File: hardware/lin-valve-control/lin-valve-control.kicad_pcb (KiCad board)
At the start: 4 copper layers, 55.6 x 43.2 mm, 65 parts, among them J1 UPDI, J2 I2C LCD, J3 Screw_Terminal_01x03, J4 Screw_Terminal_01x05, Q1 2N7002, Q2 2N7002, U1 TJA1021T, U2 ATtiny824-X, U3 PCA9536DP, U4 LTC3203BEDD-PBF, U5 BD9G341EFJ, U6 TCA9534, U7 DRV8801PWP

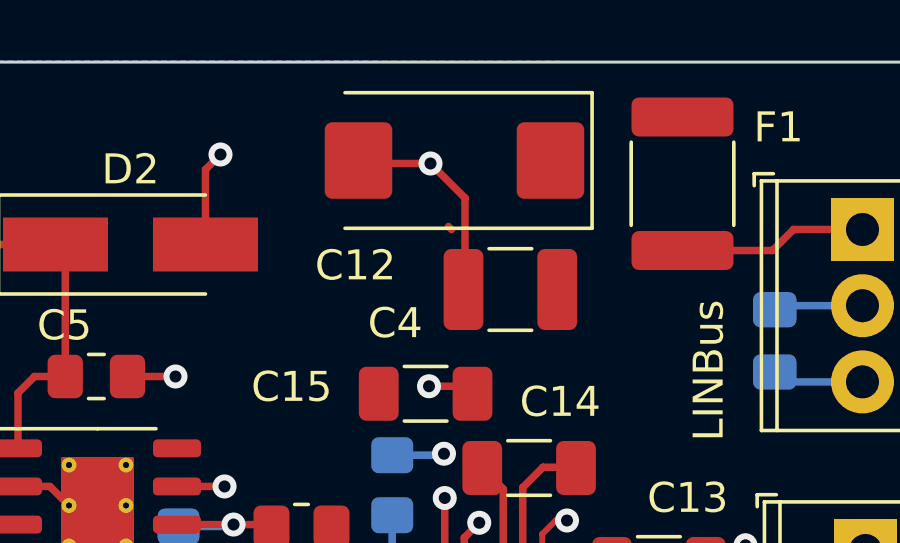
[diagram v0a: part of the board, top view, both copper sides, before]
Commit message: Add firmware for lin-coolant-temperature, cleanup layout
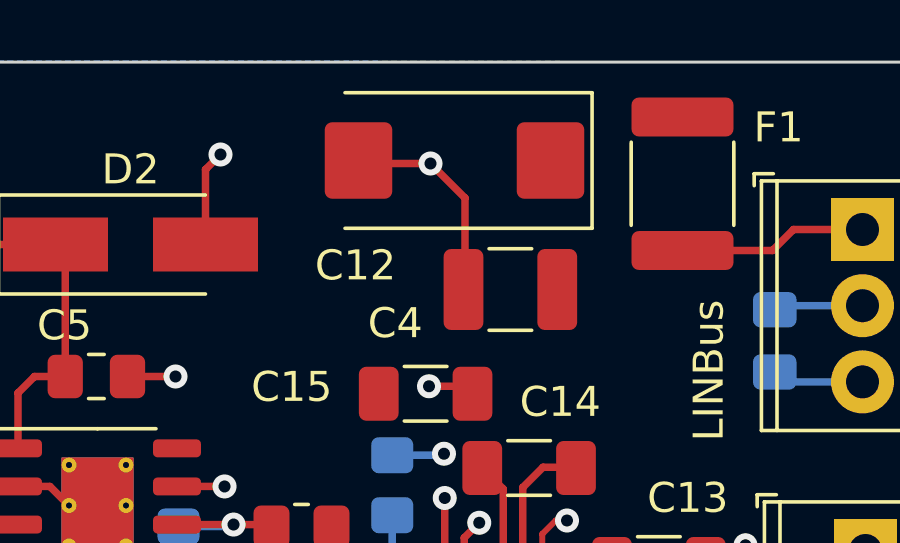
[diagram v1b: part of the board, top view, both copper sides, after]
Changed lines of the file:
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@@
   (segment (start 218.925 97.85) (end 218.9 97.875) (width 0.25) (layer "F.Cu") (net 20))
   (segment (start 218.9 97.875) (end 216.4 97.875) (width 0.25) (layer "F.Cu") (net 20))
-  (segment (start 211 64) (end 210.9 63.9) (width 0.25) (layer "F.Cu") (net 21))
   (segment (start 216.4 91.84) (end 216.36 91.8) (width 0.25) (layer "F.Cu") (net 22))
   (segment (start 216.4 94.575) (end 216.4 91.84) (width 0.25) (layer "F.Cu") (net 22))

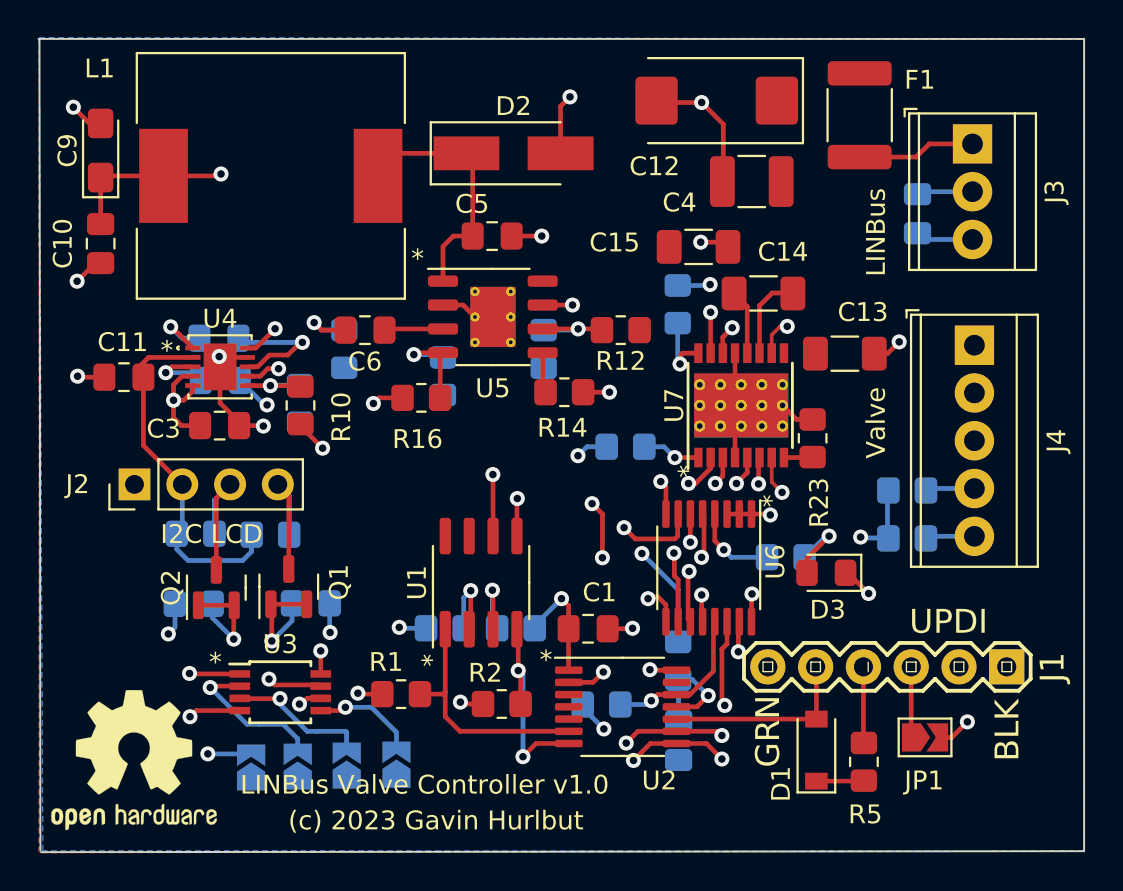
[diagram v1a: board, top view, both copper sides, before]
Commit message: Rework valve-controller board, simplify firmware
- linbus_interface and linbus_registers moved to the common lib.
- reworked them all to compile again
- removing PCA9536 from all boards, adding the voltage reg. module
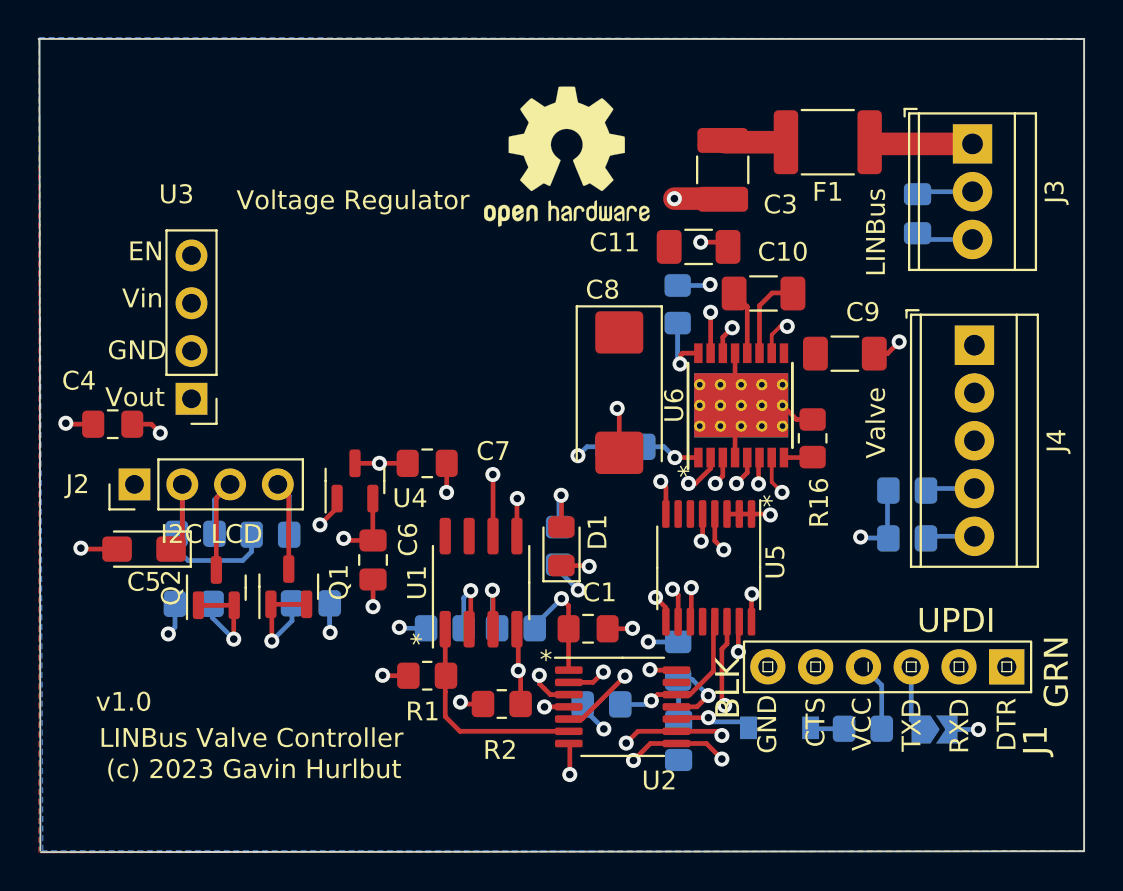
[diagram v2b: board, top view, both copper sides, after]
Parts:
- removed the C10 at (178.3, 69.3)
- removed the C11 at (179.6, 76.4)
- removed the C8 at (184.6, 74.3)
- removed the C9 at (178.3, 64.3)
- removed the D2 at (200.3, 64.5)
- removed D3: LED, LED_SMD:LED_0805_2012Metric_Pad1.15x1.40mm_HandSolder
- removed JP2: A3, Jumper:SolderJumper-2_P1.3mm_Open_TrianglePad1.0x1.5mm
- removed JP3: A2, Jumper:SolderJumper-2_P1.3mm_Open_TrianglePad1.0x1.5mm
- removed JP4: A1, Jumper:SolderJumper-2_P1.3mm_Open_TrianglePad1.0x1.5mm
- removed JP5: A0, Jumper:SolderJumper-2_P1.3mm_Open_TrianglePad1.0x1.5mm
- removed L1: 33uH 5A 88mOhm, Beirdo:PM4346.333NLT
- removed the R10 at (189.0, 77.9)
- removed the R11 at (188.9, 77.8)
- removed the R12 at (206.0, 73.9)
- removed the R13 at (201.9, 74.9)
- removed the R14 at (203.0, 77.2)
- removed the R15 at (191.3, 74.9)
- removed the R16 at (195.4, 77.5)
- removed the R17 at (196.6, 76.3)
- removed R25: 330, Resistor_SMD:R_0805_2012Metric_Pad1.20x1.40mm_HandSolder
- removed the U5 at (199.2, 73.2)
- added D1: LED, LED_SMD:LED_0805_2012Metric_Pad1.15x1.40mm_HandSolder, F.Cu at (202.8, 85.4)
- added R5: 330, Resistor_SMD:R_0805_2012Metric_Pad1.20x1.40mm_HandSolder, B.Cu at (202.7, 85.4)
- C3: value 2.2uF -> 10uF 100V; footprint Capacitor_SMD:C_0805_2012Metric_Pad1.18x1.45mm_HandSolder -> Capacitor_SMD:C_1210_3225Metric_Pad1.33x2.70mm_HandSolder
- C4: value 10uF 100V -> 1uF; footprint Capacitor_SMD:C_1210_3225Metric_Pad1.33x2.70mm_HandSolder -> Capacitor_SMD:C_0805_2012Metric_Pad1.18x1.45mm_HandSolder
- C5: value 100nF -> 100uF Ta 6V; footprint Capacitor_SMD:C_0805_2012Metric_Pad1.18x1.45mm_HandSolder -> Capacitor_Tantalum_SMD:CP_EIA-3216-10_Kemet-I_Pad1.58x1.35mm_HandSolder
- C6: value 10nF -> 1uF
- C7: value 2.2uF -> 10uF; moved to F.Cu
- D2: renamed from D1; moved to B.Cu
- J1: footprint Beirdo:FTDI_BASIC -> Beirdo:FTDI-TARGET
- JP1: moved to B.Cu
- R6: renamed from R5; moved to B.Cu
- U3: value PCA9536DP -> Voltage Regulator; footprint Package_SO:TSSOP-8_3x3mm_P0.65mm -> Beirdo:Switching_Regulator_Module
- U4: value LTC3203BEDD-PBF -> MCP1754S-3302xCB; footprint UltraLibrarian:LTC3203BEDD-PBF -> Package_TO_SOT_SMD:SOT-23
- moved REF** 39.5 mm to (203.1, 64.7)
- moved C4 36.3 mm to (179.0, 78.9)
- moved C3 30.0 mm to (211.4, 65.4), turned to -90 degrees
- moved C5 24.9 mm to (180.7, 85.5)
- moved C8 16.4 mm to (205.9, 77.2), turned to -90 degrees
- moved U3 16.2 mm to (183.2, 77.6), turned to 180 degrees
- moved C6 12.2 mm to (192.8, 86.1), turned to -90 degrees
- moved C7 11.8 mm to (195.7, 81.0), turned to 0 degrees
- moved U4 9.39 mm to (191.9, 81.9), turned to 90 degrees
- moved D2 2.29 mm to (214.4, 95.0), turned to 180 degrees
- moved F1 2.22 mm to (217.0, 63.9), turned to 180 degrees
- moved R6 1.76 mm to (218.9, 95.1), turned to 0 degrees
- moved R1 1.70 mm to (195.7, 92.3)
- moved JP1 0.66 mm to (222.7, 95.1)
- renumbered C14 to C10, C15 to C11, C16 to C12, C12 to C8, C13 to C9, R9 to R10, R18 to R11, R19 to R12, R20 to R13, R21 to R14, R22 to R15, R23 to R16, R24 to R17, R6 to R7, R7 to R8, R8 to R9, U6 to U5, U7 to U6
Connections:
- C3 pad 1: +3V3 -> +12V
- C4 pad 1: +12V -> +5V
- C5 pad 1: Net-(C5-Pad1) -> +5V
- C5 pad 2: Net-(C5-Pad2) -> GND
- C6 pad 1: Net-(C6-Pad1) -> +3V3
- C6 pad 2: Net-(C6-Pad2) -> GND
- C7 pad 1: Net-(C7-Pad1) -> +5V
- C7 pad 2: Net-(C7-Pad2) -> GND
- Q1 pad 1: SCL3V -> SCL
- Q1 pad 2: SCL3V -> SCL
- Q2 pad 1: SDA3V -> SDA
- Q2 pad 2: SDA3V -> SDA
- R10 pad 2: SCL3V -> SCL
- R9 pad 2: SDA3V -> SDA
- U2 pad 3: unconnected-(U2-Pad3) -> ~{LIN_SLP}
- U2 pad 4: unconnected-(U2-Pad4) -> ~{LIN_WAKE}
- U2 pad 5: unconnected-(U2-Pad5) -> Net-(U2-Pad5)
- U2 pad 8: SDA3V -> SDA
- U2 pad 9: SCL3V -> SCL
- U3 pad 1: Net-(JP5-Pad2) -> +5V
- U3 pad 2: Net-(JP4-Pad2) -> GND
- U3 pad 3: Net-(JP3-Pad2) -> +12V
- U3 pad 4: GND -> unconnected-(U3-Pad4)
- U4 pad 1: Net-(C8-Pad1) -> GND
- U4 pad 2: +5V -> +3V3
- U4 pad 3: Net-(C7-Pad2) -> +5V
- U5 pad 10: ~{FAULT} -> ~{VALVE_OPEN}
- U5 pad 11: ~{LIN_SLP} -> ~{FAULT}
- U5 pad 12: ~{LIN_WAKE} -> unconnected-(U5-Pad12)
- U5 pad 14: SCL3V -> SCL
- U5 pad 15: SDA3V -> SDA
- U5 pad 4: Net-(U6-Pad4) -> ENABLE
- U5 pad 5: ENABLE -> ~{SLEEP}
- U5 pad 6: ~{SLEEP} -> unconnected-(U5-Pad6)
- U5 pad 7: ~{VALVE_CLOSED} -> unconnected-(U5-Pad7)
- U5 pad 9: ~{VALVE_OPEN} -> ~{VALVE_CLOSED}
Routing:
- net SDA3V: track 47.7 -> 0.00 mm, vias 5 -> 0
- net SDA: track 0.00 -> 43.1 mm, vias 0 -> 4
- net SCL3V: track 41.5 -> 0.00 mm, vias 5 -> 0
- net SCL: track 0.00 -> 39.2 mm, vias 0 -> 4
- net +3V3: track 47.7 -> 29.8 mm, vias 18 -> 13
- net GND: track 49.2 -> 33.7 mm, vias 16 -> 14
- net Net-(C5-Pad2): track 13.4 -> 0.00 mm
- net Net-(U2-Pad5): track 0.00 -> 11.4 mm, vias 0 -> 2
- net Net-(JP5-Pad2): track 9.66 -> 0.00 mm, vias 2 -> 0
- net Net-(C7-Pad1): track 8.57 -> 0.00 mm, vias 2 -> 0
- net Net-(JP4-Pad2): track 8.13 -> 0.00 mm, vias 1 -> 0
- net Net-(JP3-Pad2): track 7.65 -> 0.00 mm, vias 1 -> 0
- net Net-(C5-Pad1): track 7.53 -> 0.00 mm, vias 2 -> 0
- net Net-(C8-Pad2): track 6.96 -> 0.00 mm, vias 1 -> 0
- net ~{LIN_SLP}: track 19.0 -> 13.3 mm
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- added copper zone on In1.Cu, net +5V
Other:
- board text added: "LINBus Valve Controller"
- board text added: "v1.0"
- board text removed: "LINBus Valve Controller v1.0"
